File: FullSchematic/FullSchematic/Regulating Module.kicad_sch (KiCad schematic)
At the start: 5 parts, among them U2 LM1117-3.3

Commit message: completed and generated BOM
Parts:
- added R16, R17: 0, symbol Device:R_US
- U2: JLCPCB Part # C126027 -> C5337196; Price 0.146 -> 0.072; Price ( 1 board) 0.146 -> 0.072; Price (5 boards) 0.73 -> 0.36
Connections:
- net Vboard: now also R17.2; no longer C4.1, R3.1, U2.2 (VO)
- net at C3.1, U2.3 (VI): now also R16.2; no longer Qrevpol.3 (S)
- new net: C4.1, R17.1, R3.1, U2.2 (VO)
- new net: Qrevpol.3 (S), R16.1
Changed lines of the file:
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@@
   (junction (at 142.24 92.71) (diameter 0) (color 0 0 0 0)
   )
+  (junction (at 133.35 102.87) (diameter 0) (color 0 0 0 0)
+  )
   (junction (at 116.84 92.71) (diameter 0) (color 0 0 0 0)
   )
-  (junction (at 133.35 102.87) (diameter 0) (color 0 0 0 0)
-  )
   (wire (pts (xy 96.52 92.71) (xy 96.52 90.17))
     (stroke (width 0) (type default))
@@
     (stroke (width 0) (type default))
   )
+  (wire (pts (xy 110.49 92.71) (xy 116.84 92.71))
+    (stroke (width 0) (type default))
+  )
   (wire (pts (xy 133.35 102.87) (xy 133.35 110.49))
     (stroke (width 0) (type default))
@@
     (stroke (width 0) (type default))
   )
-  (wire (pts (xy 96.52 92.71) (xy 116.84 92.71))
-    (stroke (width 0) (type default))
-  )
-  (wire (pts (xy 146.05 92.71) (xy 154.94 92.71))
+  (wire (pts (xy 146.05 92.71) (xy 162.56 92.71))
     (stroke (width 0) (type default))
   )
@@
     (stroke (width 0) (type default))
   )
+  (wire (pts (xy 170.18 92.71) (xy 177.8 92.71))
+    (stroke (width 0) (type default))
+  )
   (wire (pts (xy 116.84 97.79) (xy 116.84 100.33))
+    (stroke (width 0) (type default))
+  )
+  (wire (pts (xy 96.52 92.71) (xy 102.87 92.71))
     (stroke (width 0) (type default))
   )
@@
     (effects (font (size 0.8 0.8)) (justify left bottom))
   )
-  (hierarchical_label "Vboard" (shape output) (at 154.94 92.71 0) (fields_autoplaced)
+  (hierarchical_label "Vboard" (shape output) (at 177.8 92.71 0) (fields_autoplaced)
     (effects (font (size 1.27 1.27)) (justify left))
-    (property "Intersheetrefs" "${INTERSHEET_REFS}" (at 154.94 92.71 0)
+    (property "Intersheetrefs" "${INTERSHEET_REFS}" (at 177.8 92.71 0)
       (effects (font (size 1.27 1.27)) hide)
     )
@@
       (effects (font (size 1.27 1.27)) hide)
     )
-    (property "Price" "0.146" (at 133.35 92.71 0)
-      (effects (font (size 1.27 1.27)) hide)
-    )
-    (property "Price ( 1 board)" "0.146" (at 133.35 92.71 0)
-      (effects (font (size 1.27 1.27)) hide)
-    )
-    (property "Price (5 boards)" "0.73" (at 133.35 92.71 0)
-      (effects (font (size 1.27 1.27)) hide)
-    )
-    (property "JLCPCB Part #" "C126027" (at 133.35 92.71 0)
+    (property "Price" "0.072" (at 133.35 92.71 0)
+      (effects (font (size 1.27 1.27)) hide)
+    )
+    (property "Price ( 1 board)" "0.072" (at 133.35 92.71 0)
+      (effects (font (size 1.27 1.27)) hide)
+    )
+    (property "Price (5 boards)" "0.36" (at 133.35 92.71 0)
+      (effects (font (size 1.27 1.27)) hide)
+    )
+    (property "JLCPCB Part #" "C5337196" (at 133.35 92.71 0)
       (effects (font (size 1.27 1.27)) hide)
     )
@@
         (path "/5dd86611-a33d-45ee-946c-01c599f30b12/58d1f368-4b84-4dfe-a353-084728cf6b07/00000000-0000-0000-0000-00006405027d"
           (reference "R9") (unit 1)
+        )
+      )
+    )
+  )
+  (symbol (lib_id "Device:R_US") (at 166.37 92.71 90) (unit 1)
+    (in_bom yes) (on_board yes) (dnp no) (fields_autoplaced)
+    (property "Reference" "R17" (at 166.37 87.63 90)
+      (effects (font (size 1.27 1.27)))
+    )
+    (property "Value" "0" (at 166.37 90.17 90)
+      (effects (font (size 1.27 1.27)))
+    )
+    (property "Footprint" "" (at 166.624 91.694 90)
+      (effects (font (size 1.27 1.27)) hide)
+    )
+    (property "Datasheet" "~" (at 166.37 92.71 0)
+      (effects (font (size 1.27 1.27)) hide)
+    )
+    (property "JLCPCB Part #" "C17888" (at 166.37 92.71 0)
+      (effects (font (size 1.27 1.27)) hide)
+    )
+    (property "Price" "0.003" (at 166.37 92.71 0)
+      (effects (font (size 1.27 1.27)) hide)
+    )
+    (property "Price ( 1 board)" "0.012" (at 166.37 92.71 0)
+      (effects (font (size 1.27 1.27)) hide)
+    )
+    (property "Price (5 boards)" "0.06" (at 166.37 92.71 0)
+      (effects (font (size 1.27 1.27)) hide)
+    )
+    (pin "1")
+    (pin "2")
+    (instances
+      (project "FullSchematic"
+        (path "/5dd86611-a33d-45ee-946c-01c599f30b12/58d1f368-4b84-4dfe-a353-084728cf6b07/00000000-0000-0000-0000-00006405027d"
+          (reference "R17") (unit 1)
         )
       )
@@
         )
       )
+    )
+  )
+  (symbol (lib_id "Device:R_US") (at 106.68 92.71 90) (unit 1)
+    (in_bom yes) (on_board yes) (dnp no)
+    (property "Reference" "R16" (at 101.6 93.98 90)
+      (effects (font (size 1.27 1.27)))
+    )
+    (property "Value" "0" (at 101.6 96.52 90)
+      (effects (font (size 1.27 1.27)))
+    )
+    (property "Footprint" "" (at 106.934 91.694 90)
+      (effects (font (size 1.27 1.27)) hide)
+    )
+    (property "Datasheet" "~" (at 106.68 92.71 0)
+      (effects (font (size 1.27 1.27)) hide)
+    )
+    (property "JLCPCB Part #" "C17888" (at 106.68 92.71 0)
+      (effects (font (size 1.27 1.27)) hide)
+    )
+    (property "Price" "0.003" (at 106.68 92.71 0)
+      (effects (font (size 1.27 1.27)) hide)
+    )
+    (property "Price ( 1 board)" "0.012" (at 106.68 92.71 0)
+      (effects (font (size 1.27 1.27)) hide)
+    )
+    (property "Price (5 boards)" "0.06" (at 106.68 92.71 0)
+      (effects (font (size 1.27 1.27)) hide)
+    )
+    (pin "1")
+    (pin "2")
+    (instances
+      (project "FullSchematic"
+        (path "/5dd86611-a33d-45ee-946c-01c599f30b12/58d1f368-4b84-4dfe-a353-084728cf6b07/00000000-0000-0000-0000-00006405027d"
+          (reference "R16") (unit 1)
+        )
+      )

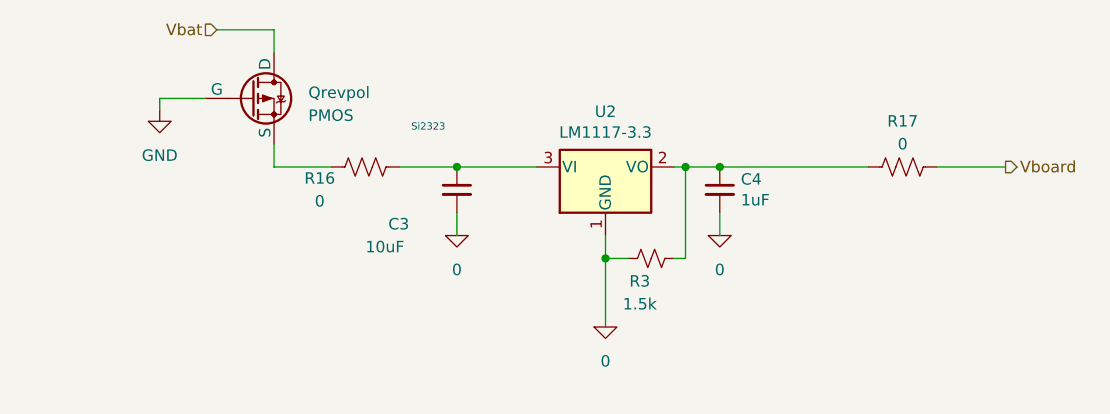
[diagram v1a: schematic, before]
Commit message: added power flags
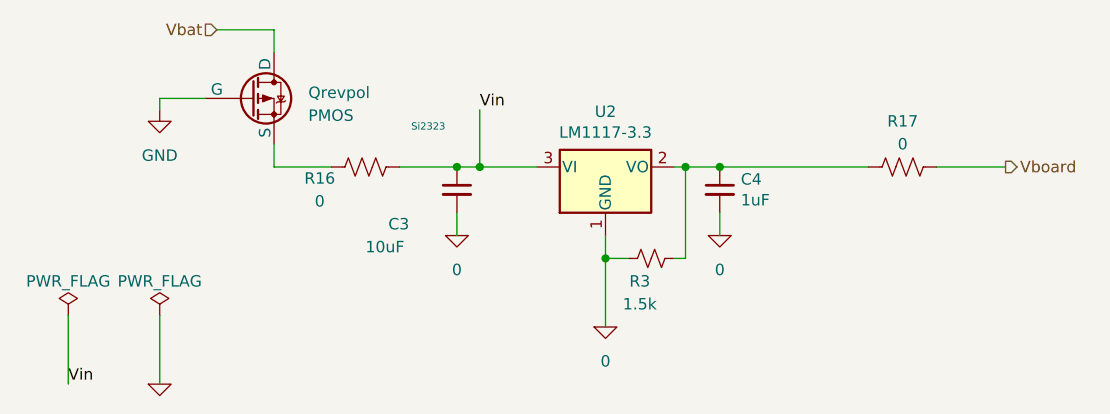
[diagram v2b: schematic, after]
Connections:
- net Vin: now reaches C3.1, R16.2, U2.3 (VI)
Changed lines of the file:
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@@
     (comment 1 "Designed By Ashik John")
   )
+  (junction (at 119.38 92.71) (diameter 0) (color 0 0 0 0)
+  )
   (junction (at 146.05 92.71) (diameter 0) (color 0 0 0 0)
   )
@@
     (stroke (width 0) (type default))
   )
+  (wire (pts (xy 83.82 109.22) (xy 83.82 116.84))
+    (stroke (width 0) (type default))
+  )
   (wire (pts (xy 133.35 100.33) (xy 133.35 102.87))
     (stroke (width 0) (type default))
   )
-  (wire (pts (xy 116.84 92.71) (xy 125.73 92.71))
+  (wire (pts (xy 116.84 92.71) (xy 119.38 92.71))
     (stroke (width 0) (type default))
   )
@@
     (stroke (width 0) (type default))
   )
+  (wire (pts (xy 119.38 92.71) (xy 125.73 92.71))
+    (stroke (width 0) (type default))
+  )
   (wire (pts (xy 170.18 92.71) (xy 177.8 92.71))
     (stroke (width 0) (type default))
@@
     (stroke (width 0) (type default))
   )
+  (wire (pts (xy 73.66 109.22) (xy 73.66 116.84))
+    (stroke (width 0) (type default))
+  )
   (wire (pts (xy 140.97 102.87) (xy 142.24 102.87))
+    (stroke (width 0) (type default))
+  )
+  (wire (pts (xy 119.38 86.36) (xy 119.38 92.71))
     (stroke (width 0) (type default))
   )
@@
   (text "Si2323" (at 111.76 88.9 0)
     (effects (font (size 0.8 0.8)) (justify left bottom))
+  )
+  (label "Vin" (at 119.38 86.36 0) (fields_autoplaced)
+    (effects (font (size 1.27 1.27)) (justify left bottom))
+  )
+  (label "Vin" (at 73.66 116.84 0) (fields_autoplaced)
+    (effects (font (size 1.27 1.27)) (justify left bottom))
   )
   (hierarchical_label "Vboard" (shape output) (at 177.8 92.71 0) (fields_autoplaced)
@@
     )
   )
+  (symbol (lib_id "Power module-rescue:0-pspice") (at 83.82 116.84 0) (unit 1)
+    (in_bom yes) (on_board yes) (dnp no)
+    (property "Reference" "#GND0106" (at 83.82 119.38 0)
+      (effects (font (size 1.27 1.27)) hide)
+    )
+    (property "Value" "0" (at 83.82 120.65 0)
+      (effects (font (size 1.27 1.27)) hide)
+    )
+    (property "Footprint" "" (at 83.82 116.84 0)
+      (effects (font (size 1.27 1.27)) hide)
+    )
+    (property "Datasheet" "~" (at 83.82 116.84 0)
+      (effects (font (size 1.27 1.27)) hide)
+    )
+    (pin "1")
+    (instances
+      (project "Power module"
+        (path "/4323dbc9-3623-4dbc-9566-44afc0929253/00000000-0000-0000-0000-00006405027d"
+          (reference "#GND0106") (unit 1)
+        )
+      )
+      (project "FullSchematic"
+        (path "/5dd86611-a33d-45ee-946c-01c599f30b12/58d1f368-4b84-4dfe-a353-084728cf6b07/00000000-0000-0000-0000-00006405027d"
+          (reference "#GND01") (unit 1)
+        )
+      )
+    )
+  )
+  (symbol (lib_id "power:PWR_FLAG") (at 73.66 109.22 0) (unit 1)
+    (in_bom yes) (on_board yes) (dnp no) (fields_autoplaced)
+    (property "Reference" "#FLG02" (at 73.66 107.315 0)
+      (effects (font (size 1.27 1.27)) hide)
+    )
+    (property "Value" "PWR_FLAG" (at 73.66 105.41 0)
+      (effects (font (size 1.27 1.27)))
+    )
+    (property "Footprint" "" (at 73.66 109.22 0)
+      (effects (font (size 1.27 1.27)) hide)
+    )
+    (property "Datasheet" "~" (at 73.66 109.22 0)
+      (effects (font (size 1.27 1.27)) hide)
+    )
+    (pin "1")
+    (instances
+      (project "FullSchematic"
+        (path "/5dd86611-a33d-45ee-946c-01c599f30b12/58d1f368-4b84-4dfe-a353-084728cf6b07/00000000-0000-0000-0000-00006405027d"
+          (reference "#FLG02") (unit 1)
+        )
+      )
+    )
+  )
   (symbol (lib_id "power:GND") (at 83.82 86.36 0) (unit 1)
     (in_bom yes) (on_board yes) (dnp no) (fields_autoplaced)
@@
         )
       )
+    )
+  )
+  (symbol (lib_id "power:PWR_FLAG") (at 83.82 109.22 0) (unit 1)
+    (in_bom yes) (on_board yes) (dnp no) (fields_autoplaced)
+    (property "Reference" "#FLG01" (at 83.82 107.315 0)
+      (effects (font (size 1.27 1.27)) hide)
+    )
+    (property "Value" "PWR_FLAG" (at 83.82 105.41 0)
+      (effects (font (size 1.27 1.27)))
+    )
+    (property "Footprint" "" (at 83.82 109.22 0)
+      (effects (font (size 1.27 1.27)) hide)
+    )
+    (property "Datasheet" "~" (at 83.82 109.22 0)
+      (effects (font (size 1.27 1.27)) hide)
+    )
+    (pin "1")
+    (instances
+      (project "FullSchematic"
+        (path "/5dd86611-a33d-45ee-946c-01c599f30b12/58d1f368-4b84-4dfe-a353-084728cf6b07/00000000-0000-0000-0000-00006405027d"
+          (reference "#FLG01") (unit 1)
+        )
+      )

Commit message: resetting
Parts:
- C3: footprint CL31A106KBHNNNE -> SpecificFootprints:CAPC1608X90N
- C4: footprint CL05A105KP5NNNC -> SpecificFootprints:CAPC1608X90N
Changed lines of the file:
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@@
       (effects (font (size 1.27 1.27)) (justify left))
     )
-    (property "Footprint" "CL31A106KBHNNNE" (at 116.84 95.25 0)
+    (property "Footprint" "SpecificFootprints:CAPC1608X90N" (at 116.84 95.25 0)
       (effects (font (size 1.27 1.27)) hide)
     )
@@
       (effects (font (size 1.27 1.27)) (justify left))
     )
-    (property "Footprint" "CL05A105KP5NNNC" (at 146.05 95.25 0)
+    (property "Footprint" "SpecificFootprints:CAPC1608X90N" (at 146.05 95.25 0)
       (effects (font (size 1.27 1.27)) hide)
     )

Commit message: Opening MicroController
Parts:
- C3: footprint SpecificFootprints:CAPC1608X90N -> CL31A106KBHNNNE
- C4: footprint SpecificFootprints:CAPC1608X90N -> CL05A105KP5NNNC
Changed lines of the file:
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@@
       (effects (font (size 1.27 1.27)) (justify left))
     )
-    (property "Footprint" "SpecificFootprints:CAPC1608X90N" (at 116.84 95.25 0)
+    (property "Footprint" "CL31A106KBHNNNE" (at 116.84 95.25 0)
       (effects (font (size 1.27 1.27)) hide)
     )
@@
       (effects (font (size 1.27 1.27)) (justify left))
     )
-    (property "Footprint" "SpecificFootprints:CAPC1608X90N" (at 146.05 95.25 0)
+    (property "Footprint" "CL05A105KP5NNNC" (at 146.05 95.25 0)
       (effects (font (size 1.27 1.27)) hide)
     )

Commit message: added more footprints
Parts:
- R16, R17: footprint (none) -> SpecificFootprints:RESC2013X65N
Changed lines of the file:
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@@
       (effects (font (size 1.27 1.27)))
     )
-    (property "Footprint" "" (at 166.624 91.694 90)
+    (property "Footprint" "SpecificFootprints:RESC2013X65N" (at 166.624 91.694 90)
       (effects (font (size 1.27 1.27)) hide)
     )
@@
       (effects (font (size 1.27 1.27)))
     )
-    (property "Footprint" "" (at 106.934 91.694 90)
-      (effects (font (size 1.27 1.27)) hide)
-    )
+    (property "Footprint" "SpecificFootprints:RESC2013X65N" (at 106.934 91.694 90)
+      (effects (font (size 1.27 1.27)) hide)
+    )

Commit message: tried to go to previous version
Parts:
- C3: footprint CL31A106KBHNNNE -> SpecificFootprints:CAPC1608X90N
- C4: footprint CL05A105KP5NNNC -> SpecificFootprints:CAPC1608X90N
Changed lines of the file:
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@@
       (effects (font (size 1.27 1.27)) (justify left))
     )
-    (property "Footprint" "CL31A106KBHNNNE" (at 116.84 95.25 0)
+    (property "Footprint" "SpecificFootprints:CAPC1608X90N" (at 116.84 95.25 0)
       (effects (font (size 1.27 1.27)) hide)
     )
@@
       (effects (font (size 1.27 1.27)) (justify left))
     )
-    (property "Footprint" "CL05A105KP5NNNC" (at 146.05 95.25 0)
+    (property "Footprint" "SpecificFootprints:CAPC1608X90N" (at 146.05 95.25 0)
       (effects (font (size 1.27 1.27)) hide)
     )

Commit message: Aimee
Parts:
- R16, R17: footprint SpecificFootprints:RESC2013X65N -> (none)
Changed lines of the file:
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@@
       (effects (font (size 1.27 1.27)))
     )
-    (property "Footprint" "SpecificFootprints:RESC2013X65N" (at 166.624 91.694 90)
+    (property "Footprint" "" (at 166.624 91.694 90)
       (effects (font (size 1.27 1.27)) hide)
     )
@@
       (effects (font (size 1.27 1.27)))
     )
-    (property "Footprint" "SpecificFootprints:RESC2013X65N" (at 106.934 91.694 90)
-      (effects (font (size 1.27 1.27)) hide)
-    )
+    (property "Footprint" "" (at 106.934 91.694 90)
+      (effects (font (size 1.27 1.27)) hide)
+    )

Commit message: adding of all footprints
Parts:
- C3, C4: footprint SpecificFootprints:CAPC1608X90N -> Library:CAPC1608X90N
- Qrevpol: footprint (none) -> Library:SOT95P237X112-3N
- R16, R17, R3: footprint (none) -> Library:RESC2013X65N
- U2: footprint (none) -> Library:SOT230P700X180-4N
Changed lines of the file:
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@@
       (effects (font (size 1.27 1.27)))
     )
-    (property "Footprint" "" (at 133.35 92.71 0)
+    (property "Footprint" "Library:SOT230P700X180-4N" (at 133.35 92.71 0)
       (effects (font (size 1.27 1.27)) hide)
     )
@@
       (effects (font (size 1.27 1.27)) (justify left))
     )
-    (property "Footprint" "SpecificFootprints:CAPC1608X90N" (at 116.84 95.25 0)
+    (property "Footprint" "Library:CAPC1608X90N" (at 116.84 95.25 0)
       (effects (font (size 1.27 1.27)) hide)
     )
@@
       (effects (font (size 1.27 1.27)) (justify left))
     )
-    (property "Footprint" "SpecificFootprints:CAPC1608X90N" (at 146.05 95.25 0)
+    (property "Footprint" "Library:CAPC1608X90N" (at 146.05 95.25 0)
       (effects (font (size 1.27 1.27)) hide)
     )
@@
       (effects (font (size 1.27 1.27)))
     )
-    (property "Footprint" "" (at 138.43 102.87 0)
+    (property "Footprint" "Library:RESC2013X65N" (at 138.43 102.87 0)
       (effects (font (size 1.27 1.27)) hide)
     )
@@
       (effects (font (size 1.27 1.27)))
     )
-    (property "Footprint" "" (at 166.624 91.694 90)
+    (property "Footprint" "Library:RESC2013X65N" (at 166.624 91.694 90)
       (effects (font (size 1.27 1.27)) hide)
     )
@@
       (effects (font (size 1.27 1.27)) (justify left))
     )
-    (property "Footprint" "" (at 99.06 82.55 0)
+    (property "Footprint" "Library:SOT95P237X112-3N" (at 99.06 82.55 0)
       (effects (font (size 1.27 1.27)) hide)
     )
@@
       (effects (font (size 1.27 1.27)))
     )
-    (property "Footprint" "" (at 106.934 91.694 90)
-      (effects (font (size 1.27 1.27)) hide)
-    )
+    (property "Footprint" "Library:RESC2013X65N" (at 106.934 91.694 90)
+      (effects (font (size 1.27 1.27)) hide)
+    )
